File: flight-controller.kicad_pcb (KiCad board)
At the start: 4 copper layers, 43 parts, among them J1 USB_C_Receptacle_USB2.0_16P, J2 Conn_Coaxial, J3 TC2030, SW1 SW_Push, U1 MIC5365-3.3YD5, U2 USBLC6-2SC6, U3 DLF162500LT-5028A1, U4 STM32WB55CEUx, U5 MPU-6050, X1 32kHz768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

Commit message: initial layout of PCB continued
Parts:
- moved SW1 82.0 mm to (82.0, 91.0)
- moved R4 70.4 mm to (75.5, 88.0)
- moved C19 69.8 mm to (75.5, 90.0)
- moved R3 66.9 mm to (78.5, 88.0)
- moved C20 66.2 mm to (83.8, 106.5), turned to 180 degrees
- moved C22 65.9 mm to (82.5, 103.7), turned to -90 degrees
- moved C21 62.8 mm to (86.8, 106.5)
- moved U2 62.6 mm to (104.8, 91.5), turned to -90 degrees
- moved U3 61.7 mm to (102.0, 108.5)
- moved C23 58.8 mm to (89.5, 104.2), turned to -90 degrees
- moved R6 53.8 mm to (90.0, 101.0)
- moved C14 53.8 mm to (107.8, 101.5), turned to 90 degrees
- moved X1 53.1 mm to (97.0, 92.0)
- moved R5 53.0 mm to (90.0, 102.2)
- moved C3 52.7 mm to (108.8, 97.0), turned to 90 degrees
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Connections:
- net Net-(U4-RF1) renamed /RF

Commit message: finished layout
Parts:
- removed J3: TC2030, Connector:Tag-Connect_TC2030-IDC-FP_2x03_P1.27mm_Vertical
- added J4: TC2030, Connector:Tag-Connect_TC2030-IDC-NL_2x03_P1.27mm_Vertical, F.Cu at (101.5, 91.8)
- moved U1 67.7 mm to (100.0, 84.8), turned to 180 degrees
- moved C2 66.7 mm to (97.0, 84.8), turned to 90 degrees
- moved C1 60.1 mm to (103.0, 85.0), turned to 90 degrees
- moved C6 54.9 mm to (105.5, 106.2), turned to 180 degrees
- moved C8 44.8 mm to (97.5, 102.0), turned to -90 degrees
- moved C13 43.8 mm to (100.8, 88.8), turned to 180 degrees
- moved C9 41.6 mm to (100.0, 95.5)
- moved C11 39.7 mm to (102.2, 105.0), turned to 180 degrees
- moved C10 34.4 mm to (107.2, 97.5), turned to 90 degrees
- moved R4 19.3 mm to (92.0, 98.0), turned to 90 degrees
- moved R3 17.8 mm to (93.2, 98.0), turned to 90 degrees
- moved C19 17.2 mm to (90.8, 98.0), turned to 90 degrees
- moved R2 12.6 mm to (111.8, 77.8), turned to 90 degrees
- moved R1 12.0 mm to (99.8, 77.8), turned to 90 degrees
- moved C12 11.8 mm to (98.5, 95.0), turned to 90 degrees
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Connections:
- net /RF renamed Net-(U4-RF1)

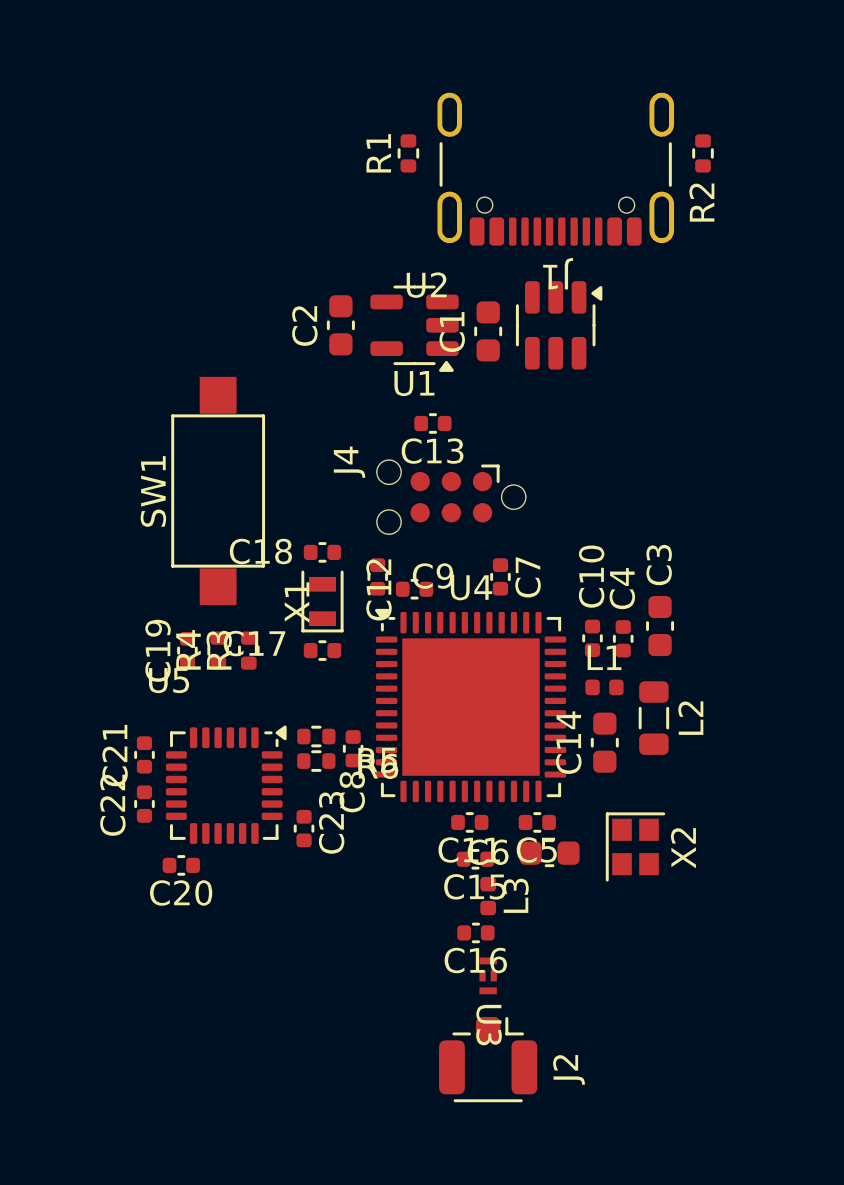
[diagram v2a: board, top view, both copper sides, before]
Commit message: begin routing, i2c layout refinement wip
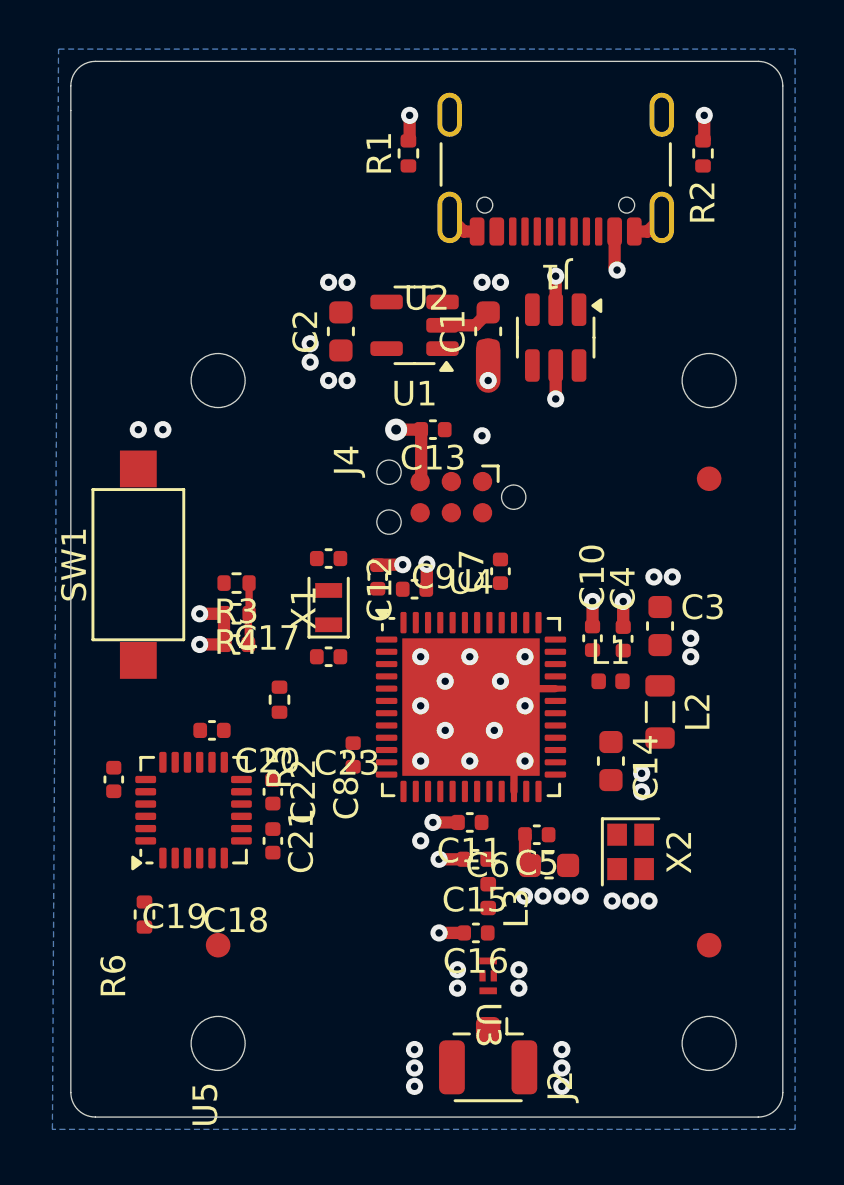
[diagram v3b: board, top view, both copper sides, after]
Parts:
- added FID1: Fiducial, Fiducial:Fiducial_1mm_Mask2mm, F.Cu at (112.0, 91.0)
- added FID2: Fiducial, Fiducial:Fiducial_1mm_Mask2mm, F.Cu at (92.0, 110.0)
- added FID3: Fiducial, Fiducial:Fiducial_1mm_Mask2mm, F.Cu at (112.0, 110.0)
- added H1: MountingHole_Pad, MountingHole:MountingHole_2.2mm_M2, F.Cu at (92.0, 114.0)
- added H2: MountingHole_Pad, MountingHole:MountingHole_2.2mm_M2, F.Cu at (112.0, 114.0)
- added H3: MountingHole_Pad, MountingHole:MountingHole_2.2mm_M2, F.Cu at (112.0, 87.0)
- added H4: MountingHole_Pad, MountingHole:MountingHole_2.2mm_M2, F.Cu at (92.0, 87.0)
- moved R6 10.1 mm to (89.0, 108.8), turned to -90 degrees
- moved C23 8.00 mm to (87.8, 103.2), turned to 90 degrees
- moved C21 6.29 mm to (94.2, 105.8), turned to -90 degrees
- moved C20 5.64 mm to (91.8, 101.2)
- moved C22 5.25 mm to (94.2, 103.8), turned to 90 degrees
- moved SW1 4.42 mm to (88.8, 94.5)
- moved R5 2.92 mm to (94.5, 100.0), turned to -90 degrees
- moved R3 2.80 mm to (92.8, 95.2), turned to 180 degrees
- moved C19 2.02 mm to (92.8, 97.8), turned to 180 degrees
- moved R4 1.68 mm to (92.8, 96.5), turned to 180 degrees
- moved U5 1.60 mm to (91.0, 104.5), turned to 90 degrees
- moved C14 0.79 mm to (108.0, 102.5), turned to -90 degrees
- moved C5 0.50 mm to (105.0, 105.5)
- moved C6 0.50 mm to (105.5, 106.8)
- moved U2 0.50 mm to (105.8, 85.2)
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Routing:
- net GND: track 0.00 -> 31.1 mm, vias 0 -> 48
- net +5V: track 0.00 -> 4.20 mm, vias 0 -> 3
- net /BOOT0: track 0.00 -> 2.51 mm
- net +3V3: track 0.00 -> 0.03 mm, vias 0 -> 12
- added copper zone on B.Cu, net +3V3
- added copper zone on In1.Cu, net GND
- added copper zone on In2.Cu, net GND
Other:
- board outline added: 29 x 43 mm

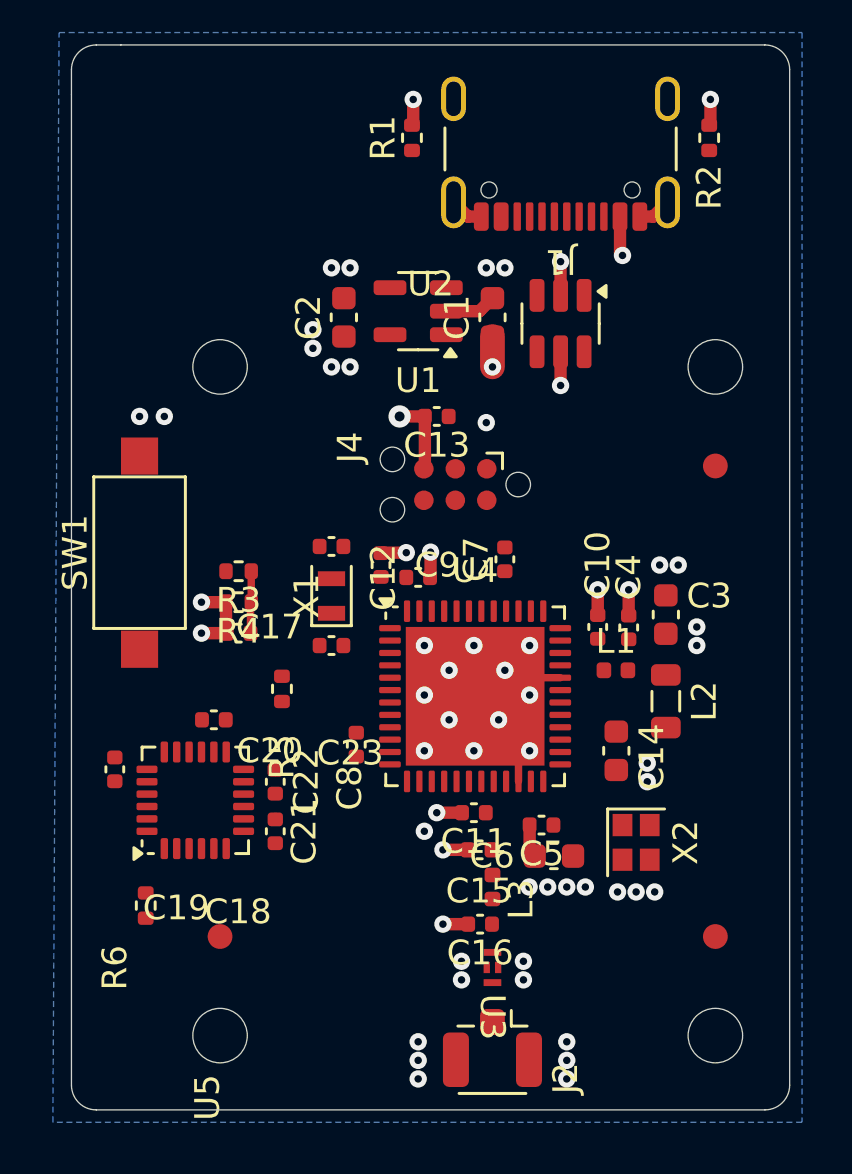
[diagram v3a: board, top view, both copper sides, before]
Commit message: Routing continued. I2C mostly fixed up
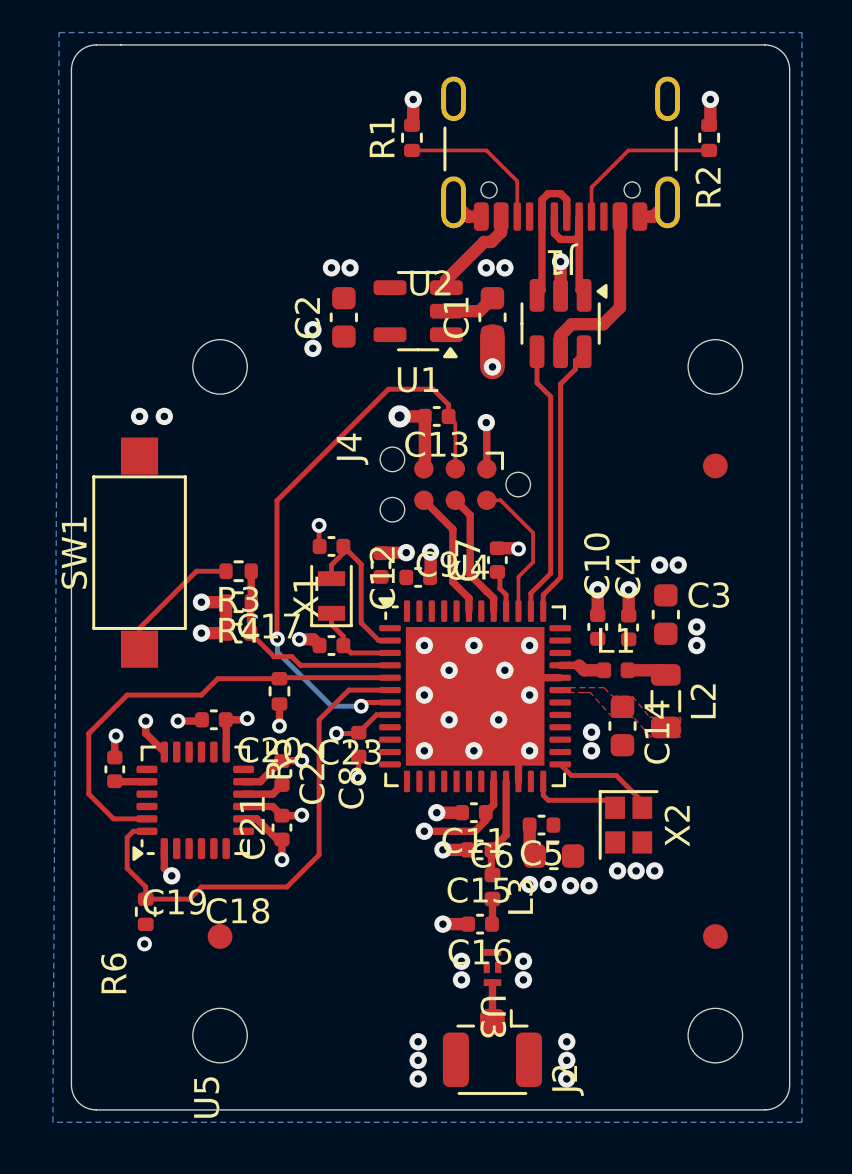
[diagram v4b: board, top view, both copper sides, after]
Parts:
- moved C14 1.03 mm to (108.2, 101.5)
- moved X2 0.76 mm to (108.5, 105.5)
- moved C22 0.44 mm to (94.5, 103.4)
- moved C21 0.31 mm to (94.5, 105.6), turned to 90 degrees
- moved C7 0.30 mm to (103.2, 94.8)
- moved R6 0.25 mm to (89.0, 109.0)
- moved R5 0.14 mm to (94.4, 100.1)
- moved C8 0.10 mm to (97.6, 102.2)
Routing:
- net /SWD_NRST: track 0.00 -> 23.4 mm, vias 0 -> 2
- net /I2C1_SDA: track 0.00 -> 20.3 mm
- net /I2C1_SCL: track 0.00 -> 18.3 mm
- net /USB_D-: track 0.00 -> 17.0 mm
- net /USB_D+: track 0.00 -> 16.9 mm
- net +3V3: track 0.03 -> 16.2 mm, vias 12 -> 15
- net GND: track 31.1 -> 44.5 mm, vias 48 -> 58
- net +5V: track 4.20 -> 12.4 mm, vias 3 -> 1
- net Net-(J1-CC1): track 0.00 -> 6.55 mm
- net /LSE_IN: track 0.16 -> 6.50 mm
- net Net-(J1-CC2): track 0.00 -> 6.19 mm
- net /BOOT0: track 2.51 -> 8.68 mm
- net /SWD_DIO: track 0.00 -> 5.82 mm
- net Net-(R3-Pad2): track 0.00 -> 5.29 mm
- net Net-(J4-SWO): track 0.00 -> 5.23 mm
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- added copper zone on F.Cu, net /SMPSFB

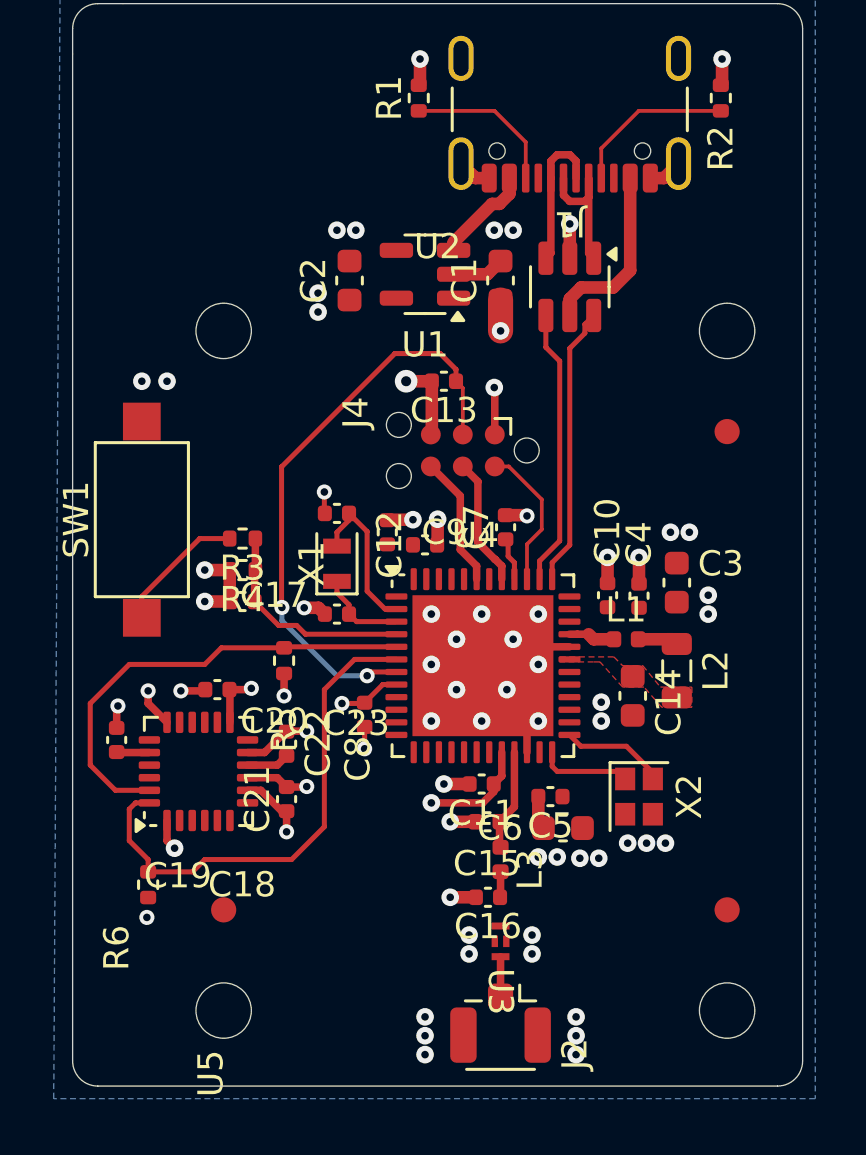
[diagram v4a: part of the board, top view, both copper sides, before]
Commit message: routing mostly complete
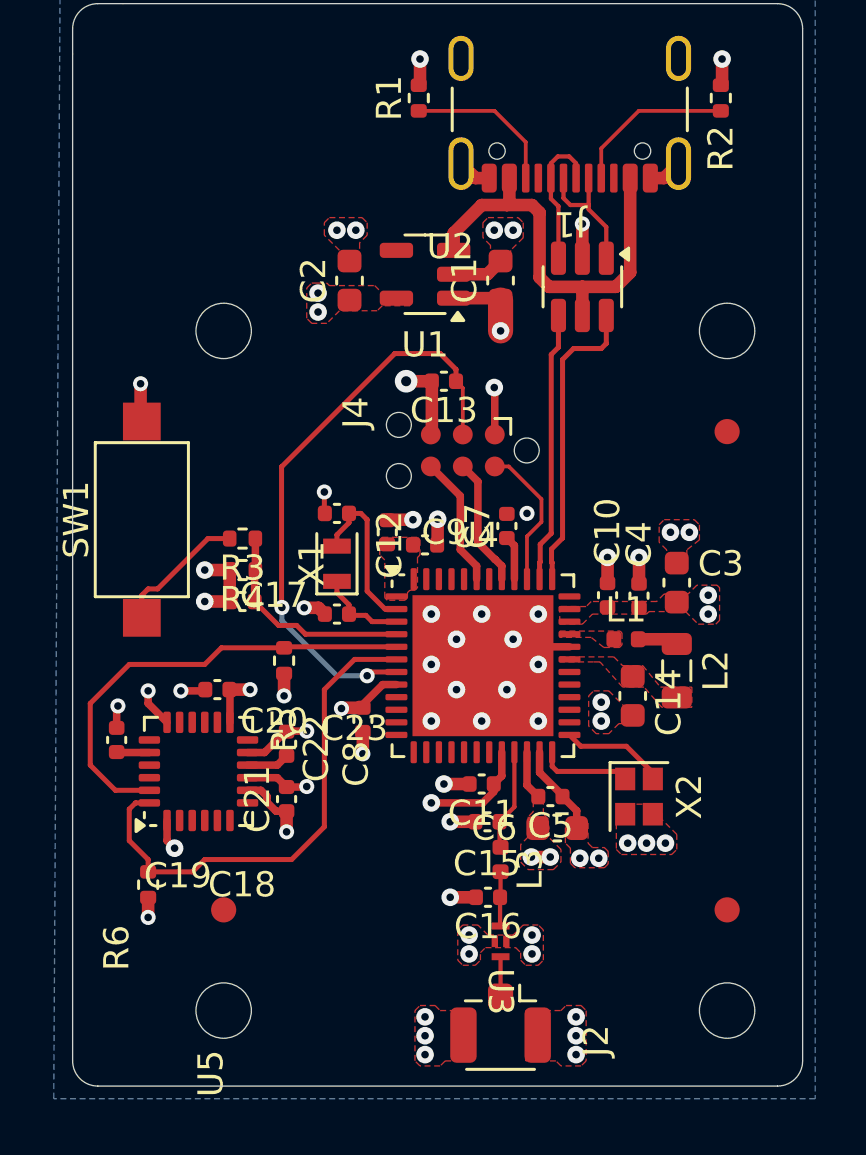
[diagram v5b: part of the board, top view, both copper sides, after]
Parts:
- moved U2 0.50 mm to (106.2, 85.2)
- moved C6 0.23 mm to (105.2, 106.8)
- moved C8 0.21 mm to (97.5, 102.5)
- moved C7 0.07 mm to (103.2, 94.8)
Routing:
- net +5V: track 12.4 -> 20.4 mm
- net +3V3: track 16.2 -> 22.7 mm, vias 15 -> 14
- net /SMPSLX: track 1.85 -> 0.00 mm
- net /RF_MATCH: track 1.02 -> 2.17 mm
- net GND: track 44.5 -> 43.6 mm
- added copper zone on F.Cu, net +3V3
- added copper zone on F.Cu, net /SMPSLX
- added copper zone on F.Cu, net GND

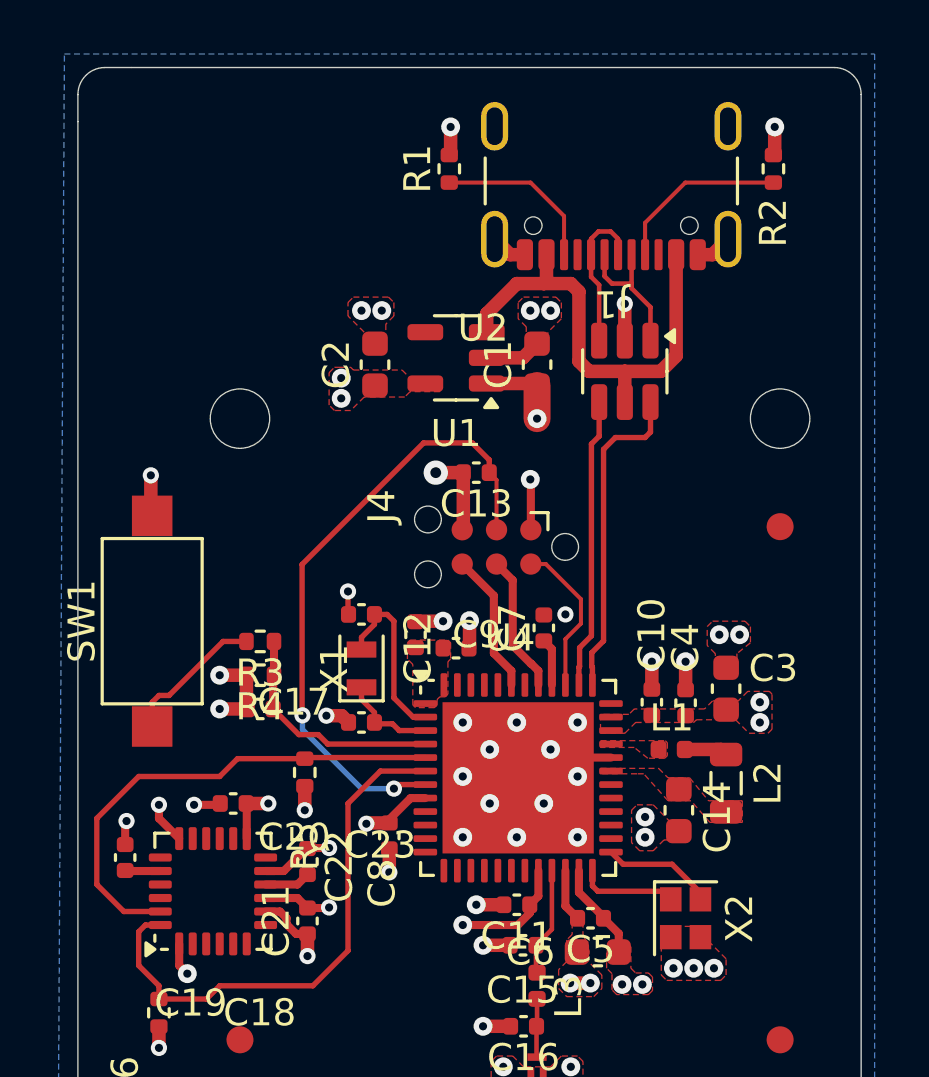
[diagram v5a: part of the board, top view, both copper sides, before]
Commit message: BOM updates, minor routing improvements
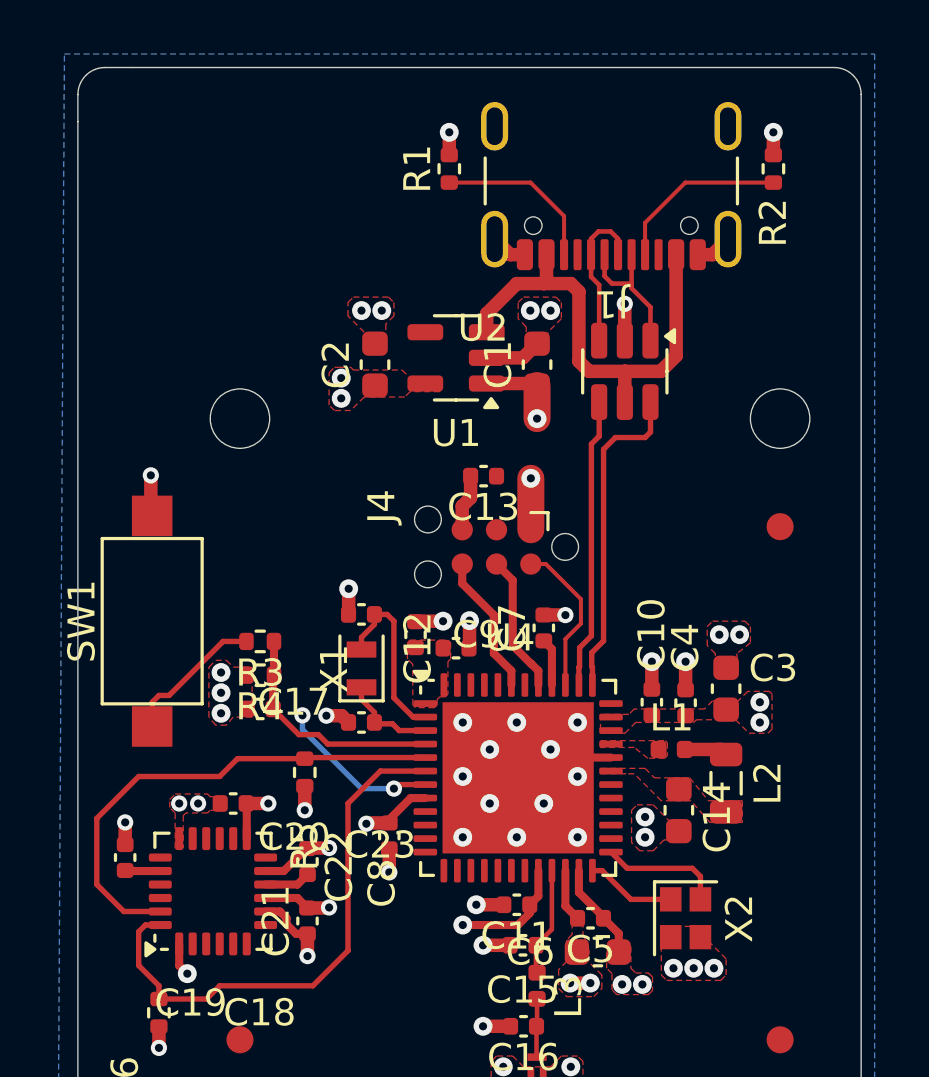
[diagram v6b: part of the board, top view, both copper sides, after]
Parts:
- moved C13 0.30 mm to (101.0, 89.1)
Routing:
- net /SWD_NRST: track 23.4 -> 6.06 mm
- net GND: track 43.6 -> 37.3 mm
